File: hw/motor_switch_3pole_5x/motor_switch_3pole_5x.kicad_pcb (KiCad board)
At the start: 2 copper layers, 93 x 89.6 mm, 167 parts, among them J1 CONN_2X1, J10 WAGO 233-504, J11 WAGO 233-504, J12 CONN-ISP-6, J13 WAGO 243-723, J14 WAGO 243-724, J15 WAGO 243-721, J16 WAGO 243-722, J17 CONN_1, J18 CONN_1, J19 tp_output_motor_0_up, J2 WAGO 2081-1122, J20 tp_output_motor_on, J21 tp_output_motor_1_up, J22 tp_output_motor_1_on, J23 tp_output_motor_2_up, J24 tp_output_motor_2_on, J25 tp_output_motor_3_up, J26 tp_output_motor_3_on, J27 tp_output_motor_4_up, J28 tp_output_motor_4_on, J29 tp_cseep, J3 WAGO 2081-1122, J30 tp_vcc, J31 tp_gnd, J32 tp_output_button_0_up, J33 tp_output_button_0_down, J34 tp_output_button_1_up, J35 tp_output_button_1_down, J36 tp_output_button_2_up, J37 tp_output_button_2_down, J38 tp_output_button_3_up, J39 tp_output_button_3_down, J4 WAGO 2081-1122, J40 tp_output_button_4_up, J41 tp_output_button_4_down, J42 tp_output_latch, J43 tp_output_data, J44 tp_output_clock, J45 tp_output_reset, J46 tp_miso, J47 tp_txden, J48 tp_txd, J49 tp_rxd, J5 WAGO 2081-1122, J6 WAGO 2081-1122, J7 WAGO 233-504, J8 WAGO 233-504, J9 WAGO 233-504, Q1 BSS138, Q10 BSS138, Q2 BSS138, Q3 BSS138, Q4 BSS138, Q5 BSS138, Q6 BSS138, Q7 BSS138, Q8 BSS138, Q9 BSS138, U1 74HC595, U2 74HC595, U3 25LC256, U4 ATMEGA328-TQFP32, U5 7,3728MHz, U6 MAX487ECSA, U7 AM1S-2405

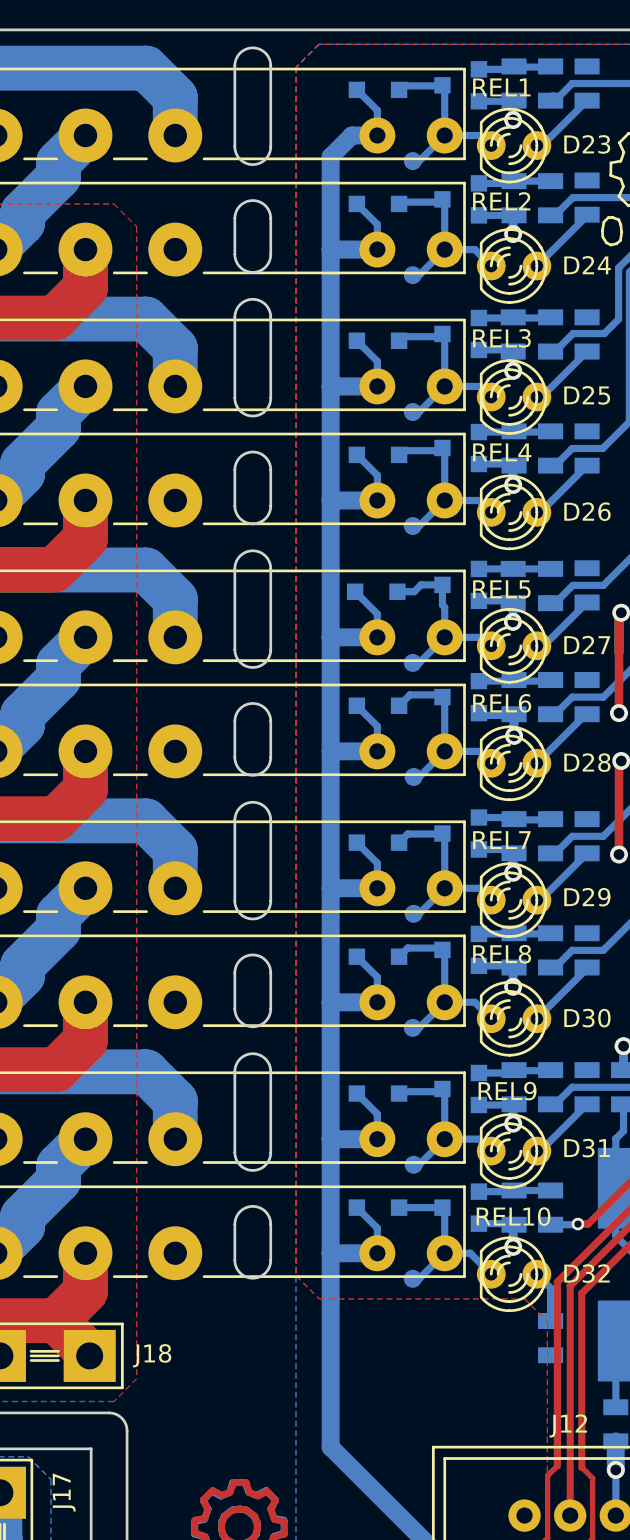
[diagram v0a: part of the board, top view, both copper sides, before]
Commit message: Update to KiCAD6: motor_switch_3pole_5x
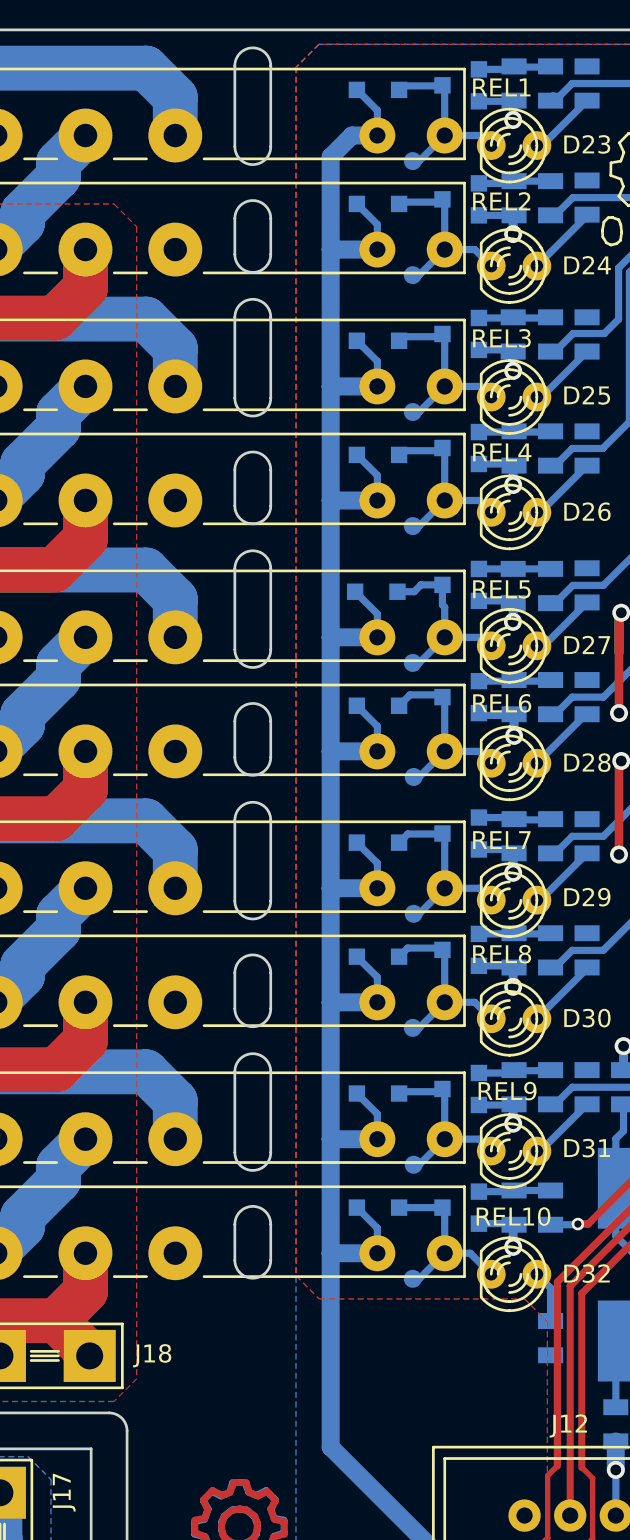
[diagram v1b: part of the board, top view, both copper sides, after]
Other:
- net class 230V removed
- net class Default removed
- net class Power removed
